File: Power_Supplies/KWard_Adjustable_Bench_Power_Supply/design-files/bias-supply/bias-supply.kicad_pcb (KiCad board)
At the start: 2 copper layers, 85.7 x 75.6 mm, 30 parts, among them J1 168VAC input, J2 To C- meter, J3 To panel jacks, Q1 MJE5731, Q2 MJE5731, Q3 KSA1013

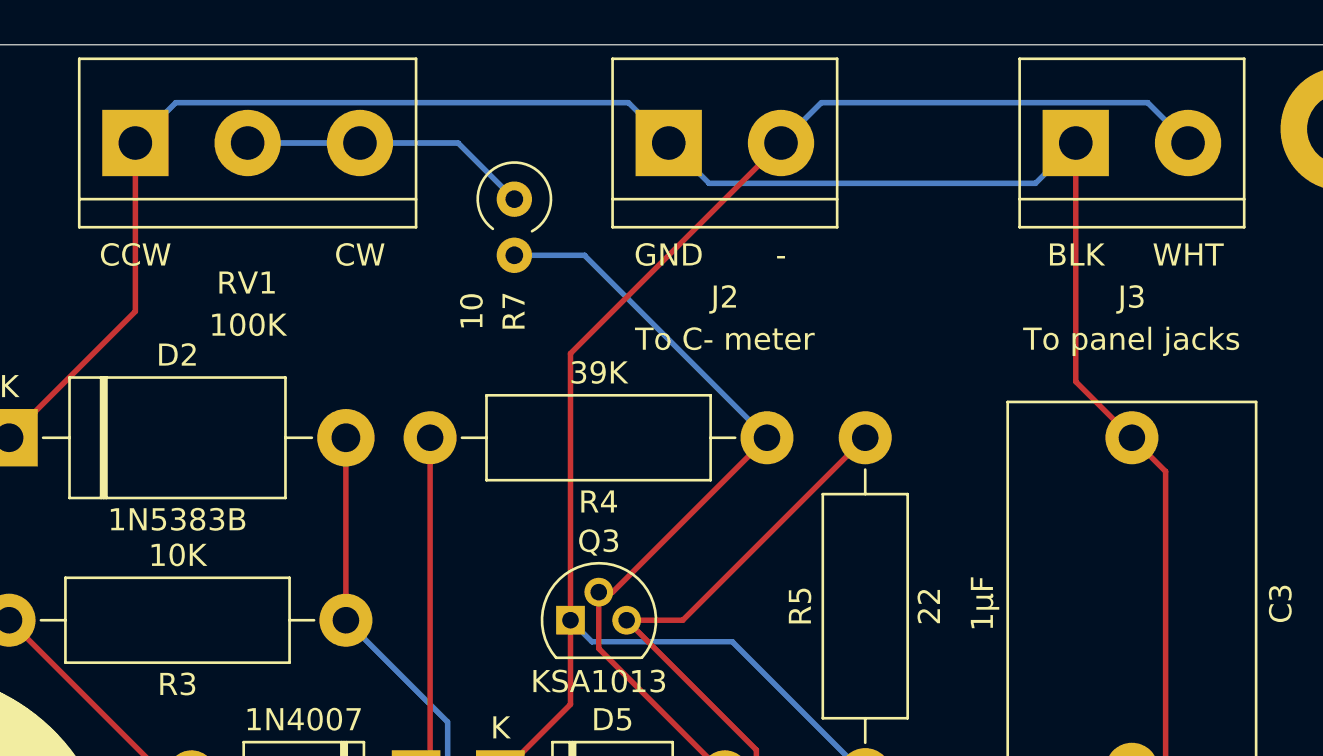
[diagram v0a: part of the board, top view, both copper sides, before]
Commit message: Make the C- meter terminal a 3-position part, with a separate one for the GND reference.
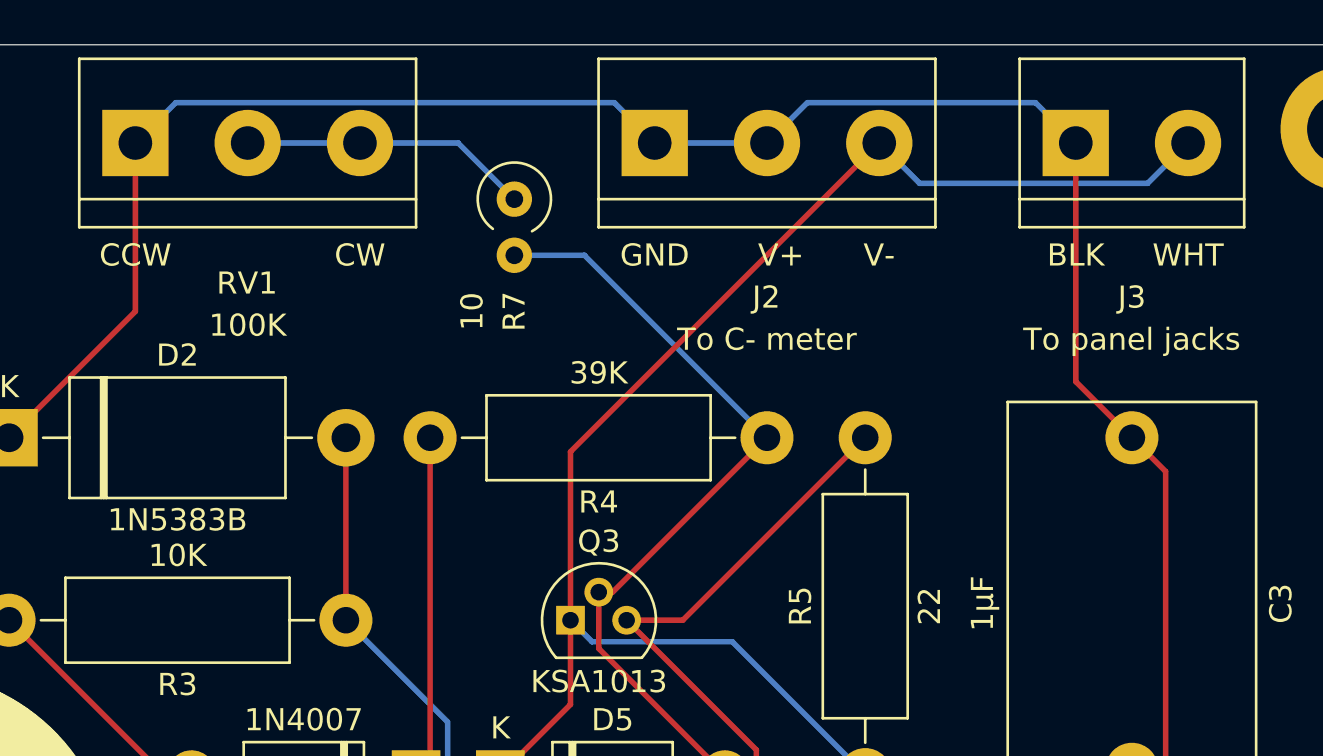
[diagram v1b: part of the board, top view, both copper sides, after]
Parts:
- J2: footprint TerminalBlock:TerminalBlock_bornier-2_P5.08mm -> TerminalBlock:TerminalBlock_bornier-3_P5.08mm
- moved J2 0.63 mm to (146.1, 64.1)
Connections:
- J2 pad 2: Net-(C3-Pad2) -> GND
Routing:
- net Net-(C3-Pad2): track 92.8 -> 90.2 mm
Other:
- board text added: "V+"
- board text added: "V-"
- board text removed: "-"

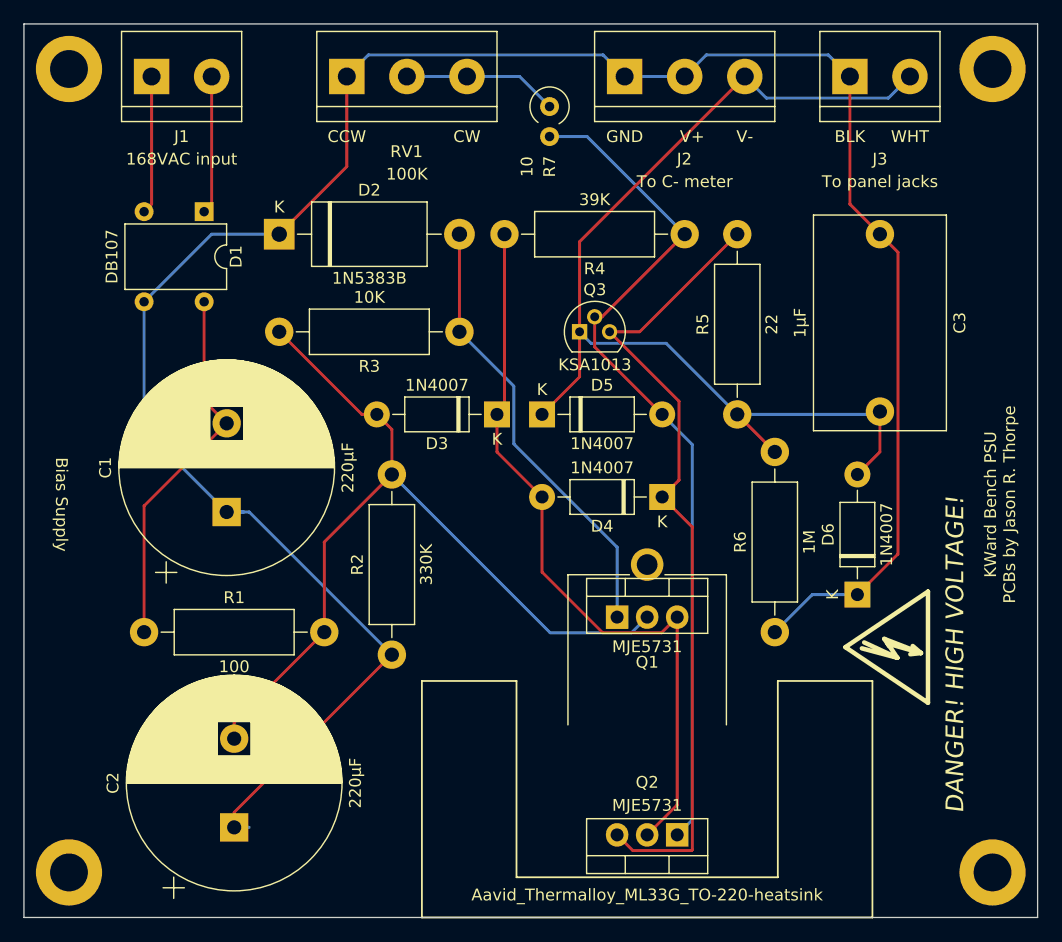
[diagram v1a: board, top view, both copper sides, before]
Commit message: Correct AC input value label, and change mounting holes to NPTH.
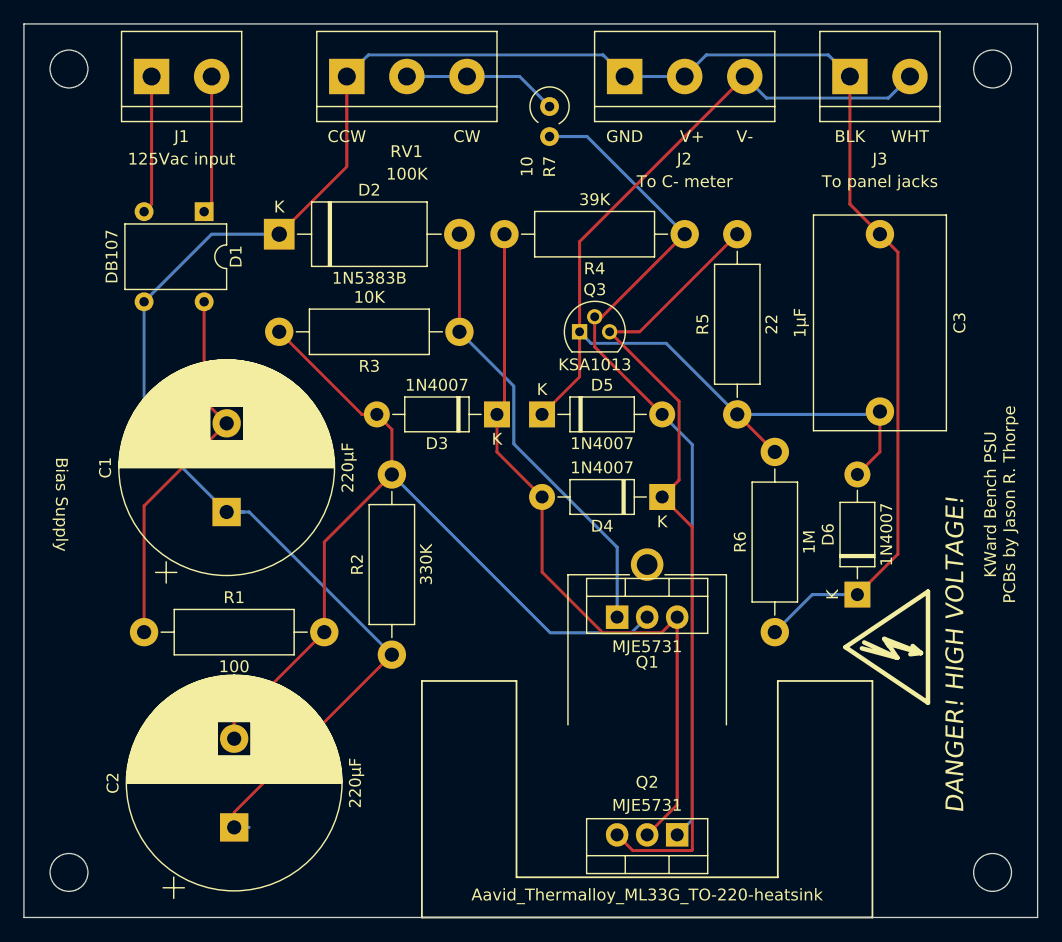
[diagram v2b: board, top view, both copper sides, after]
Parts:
- J1: value 168VAC input -> 125Vac input
- REF** (x4): value MountingHole_3.2mm_M3_DIN965_Pad -> MountingHole_3.2mm_M3_DIN965; footprint MountingHole:MountingHole_3.2mm_M3_DIN965_Pad -> MountingHole:MountingHole_3.2mm_M3_DIN965

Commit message: Final tweaks for rev 1.0.
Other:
- board text added: "Bias Supply Rev 1.0"
- board text removed: "Bias Supply"
